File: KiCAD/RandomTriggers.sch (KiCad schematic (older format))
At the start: 35 parts, among them Q1 2N3904, Q2 2N3904, U1 TL072, U2 TL072

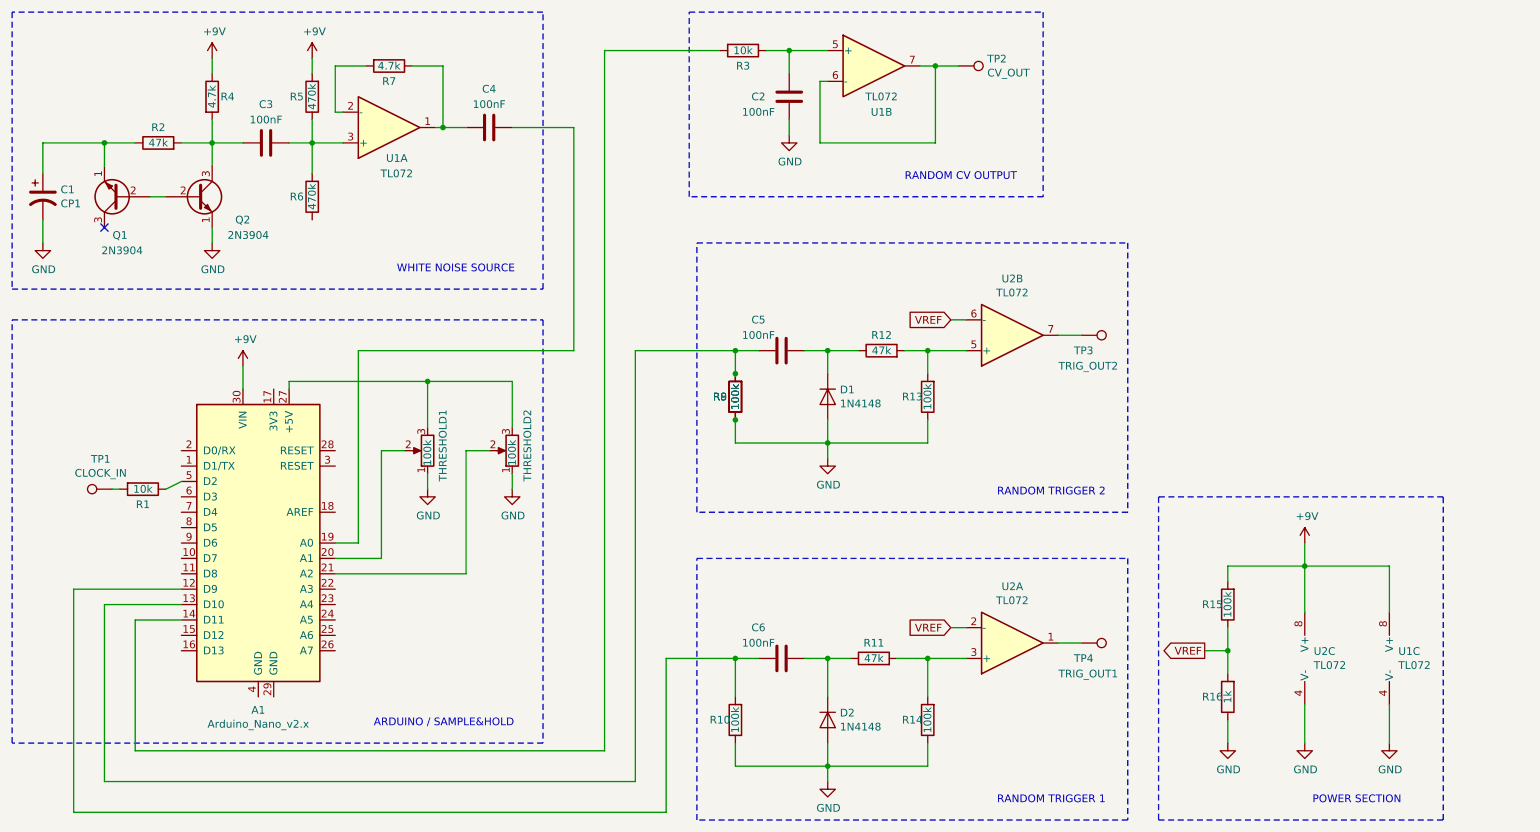
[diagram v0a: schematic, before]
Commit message: Added gate/trigger toggles
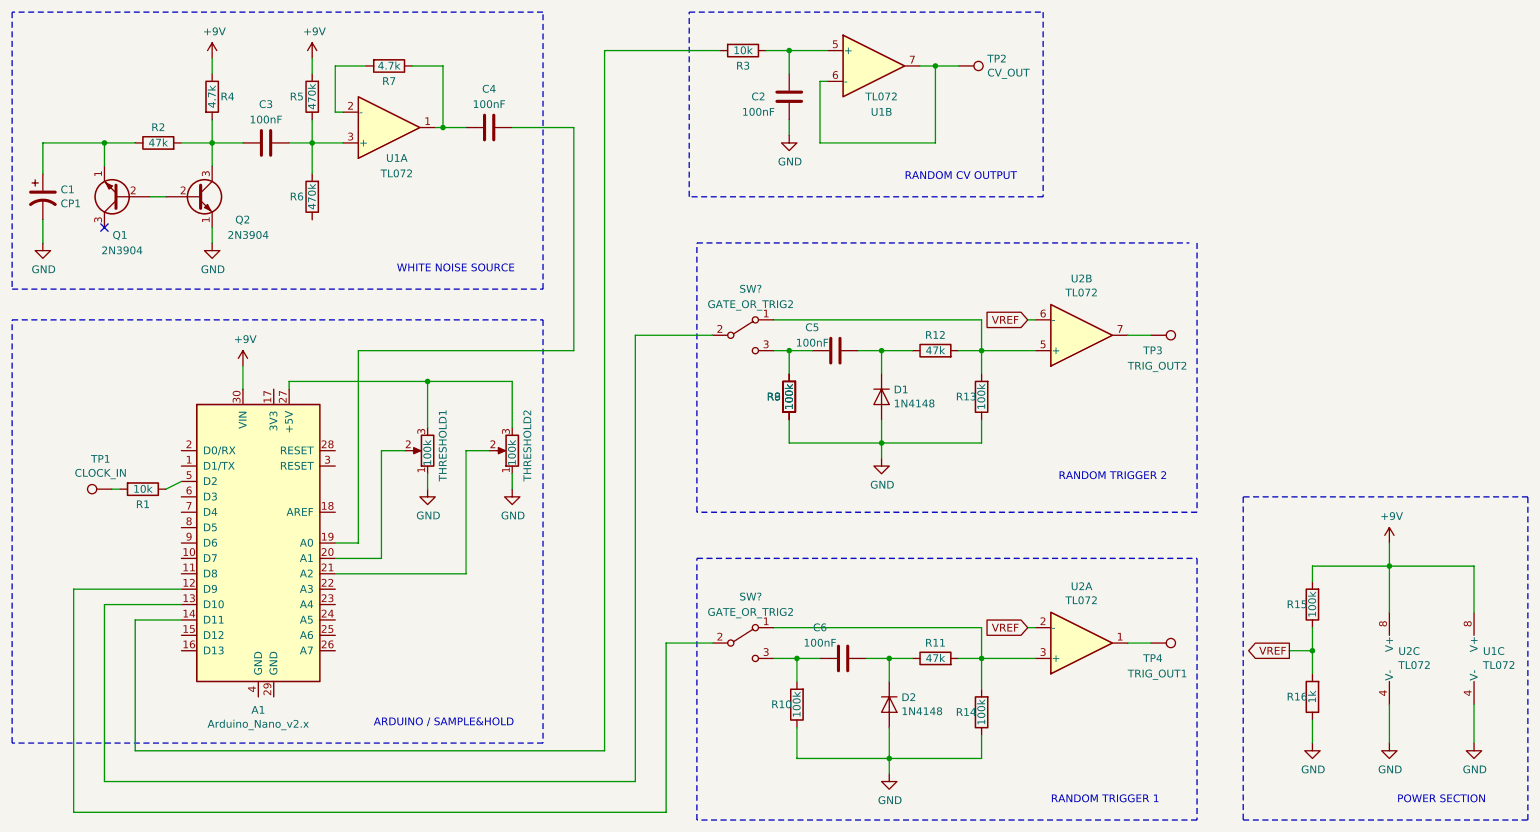
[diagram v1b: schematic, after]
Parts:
- added SW? (x2): GATE_OR_TRIG2, symbol Switch:SW_SPDT
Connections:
- net at C6.1, R10.2: now also SW?.3 (C); no longer A1.12 (D9)
- net at C5.1, R8.2, R9.2: now also SW?.3 (C); no longer A1.13 (D10)
- net at R11.2, R14.2, U2.3 (+): now also SW?.1 (A)
- net at R12.2, R13.2, U2.5 (+): now also SW?.1 (A)
- new net: A1.12 (D9), SW?.2 (B)
- new net: A1.13 (D10), SW?.2 (B)
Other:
- moved on the sheet: C5, C6, D1, D2, R10, R11, R12, R13, R14, R15, R16, R8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
